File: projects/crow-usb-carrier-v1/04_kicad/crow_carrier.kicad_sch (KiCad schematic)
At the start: 569 parts, among them J1 615008160221, J2 615008160221, J3 615008160221, J4 615008160221, J5 615008160221, J6 615008160221, J7 615008160221, J8 615008160221

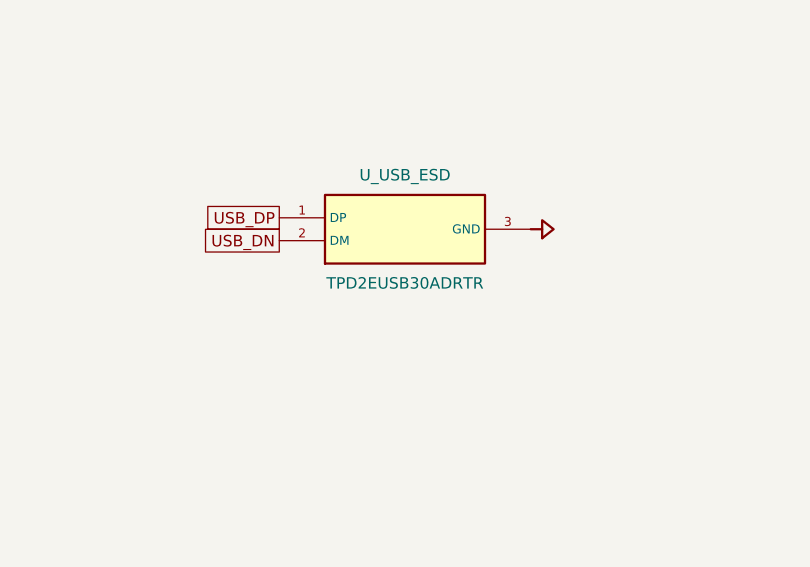
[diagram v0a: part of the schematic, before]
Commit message: crow: admit reviewed UV schematic checkpoint
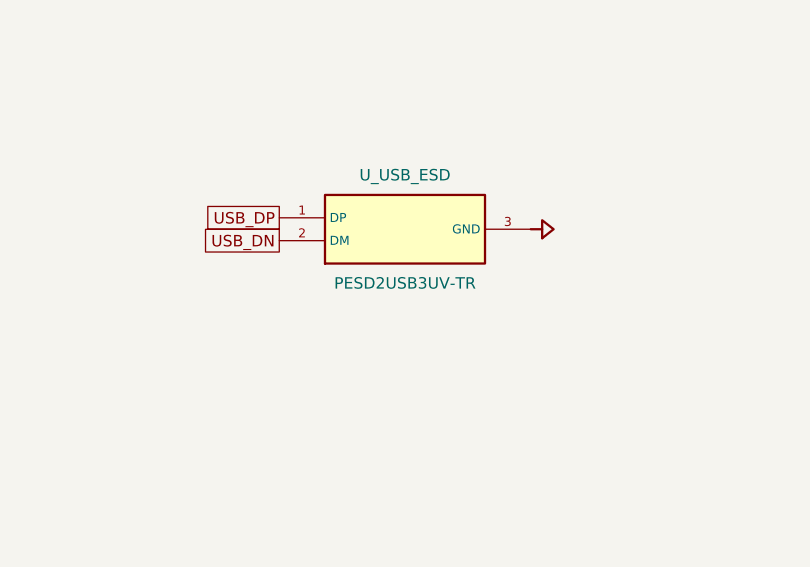
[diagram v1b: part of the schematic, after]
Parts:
- U_USB_ESD: value TPD2EUSB30ADRTR -> PESD2USB3UV-TR; footprint Package_TO_SOT_SMD:Texas_DRT-3 -> crow_usb_analog:Nexperia_PESD2USB3UV_SOT23; Manufacturer Part Number TPD2EUSB30ADRTR -> PESD2USB3UV-TR; Supplier Part Numbers {"jlcpcb": ["C94934"]} -> {"jlcpcb": ["C3704436"]}

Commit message: Adopt TI prototype schematic artifacts with guarded receipt
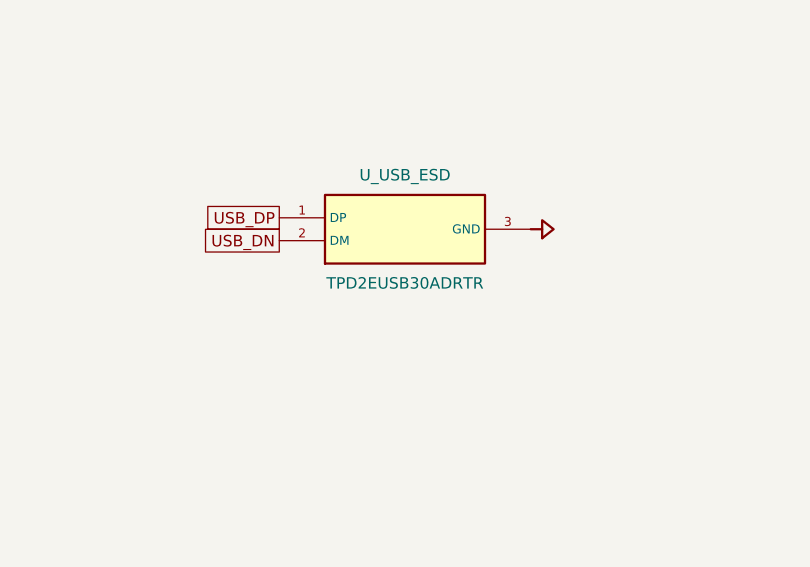
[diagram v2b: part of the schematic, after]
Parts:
- U_USB_ESD: value PESD2USB3UV-TR -> TPD2EUSB30ADRTR; footprint crow_usb_analog:Nexperia_PESD2USB3UV_SOT23 -> Package_TO_SOT_SMD:Texas_DRT-3; Manufacturer Part Number PESD2USB3UV-TR -> TPD2EUSB30ADRTR; Supplier Part Numbers {"jlcpcb": ["C3704436"]} -> {"jlcpcb": ["C94934"]}
